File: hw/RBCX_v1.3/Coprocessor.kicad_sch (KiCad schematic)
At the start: 27 parts

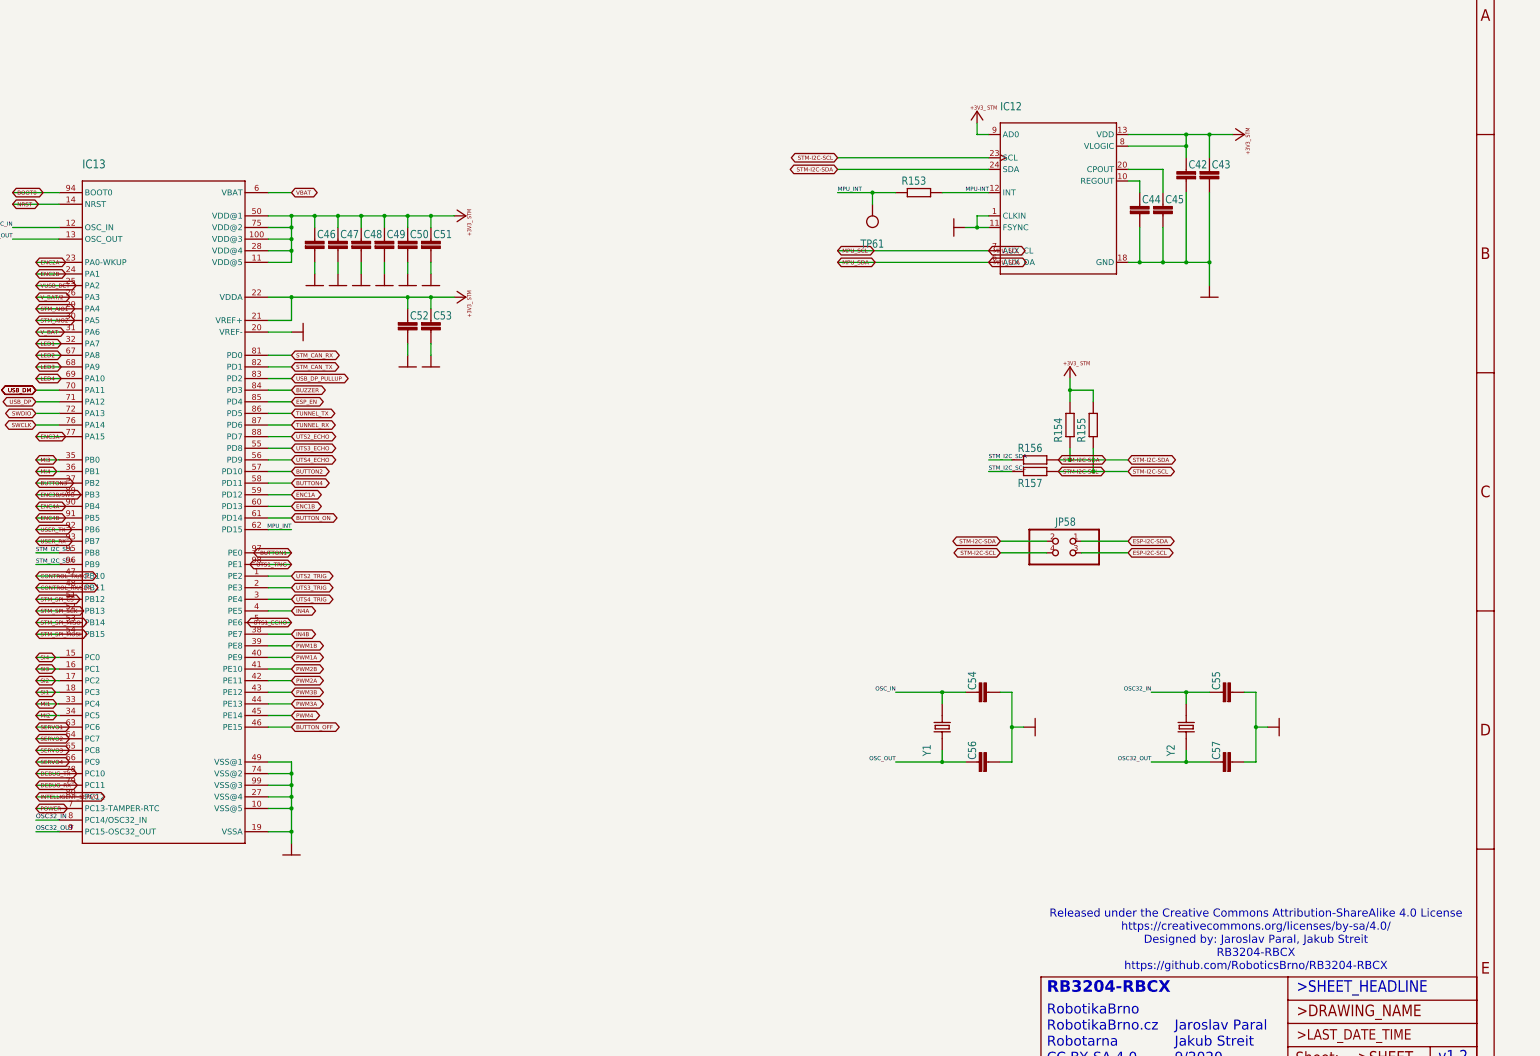
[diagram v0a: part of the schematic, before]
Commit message: Remove stepdowns, Micro-USB; fixup region names
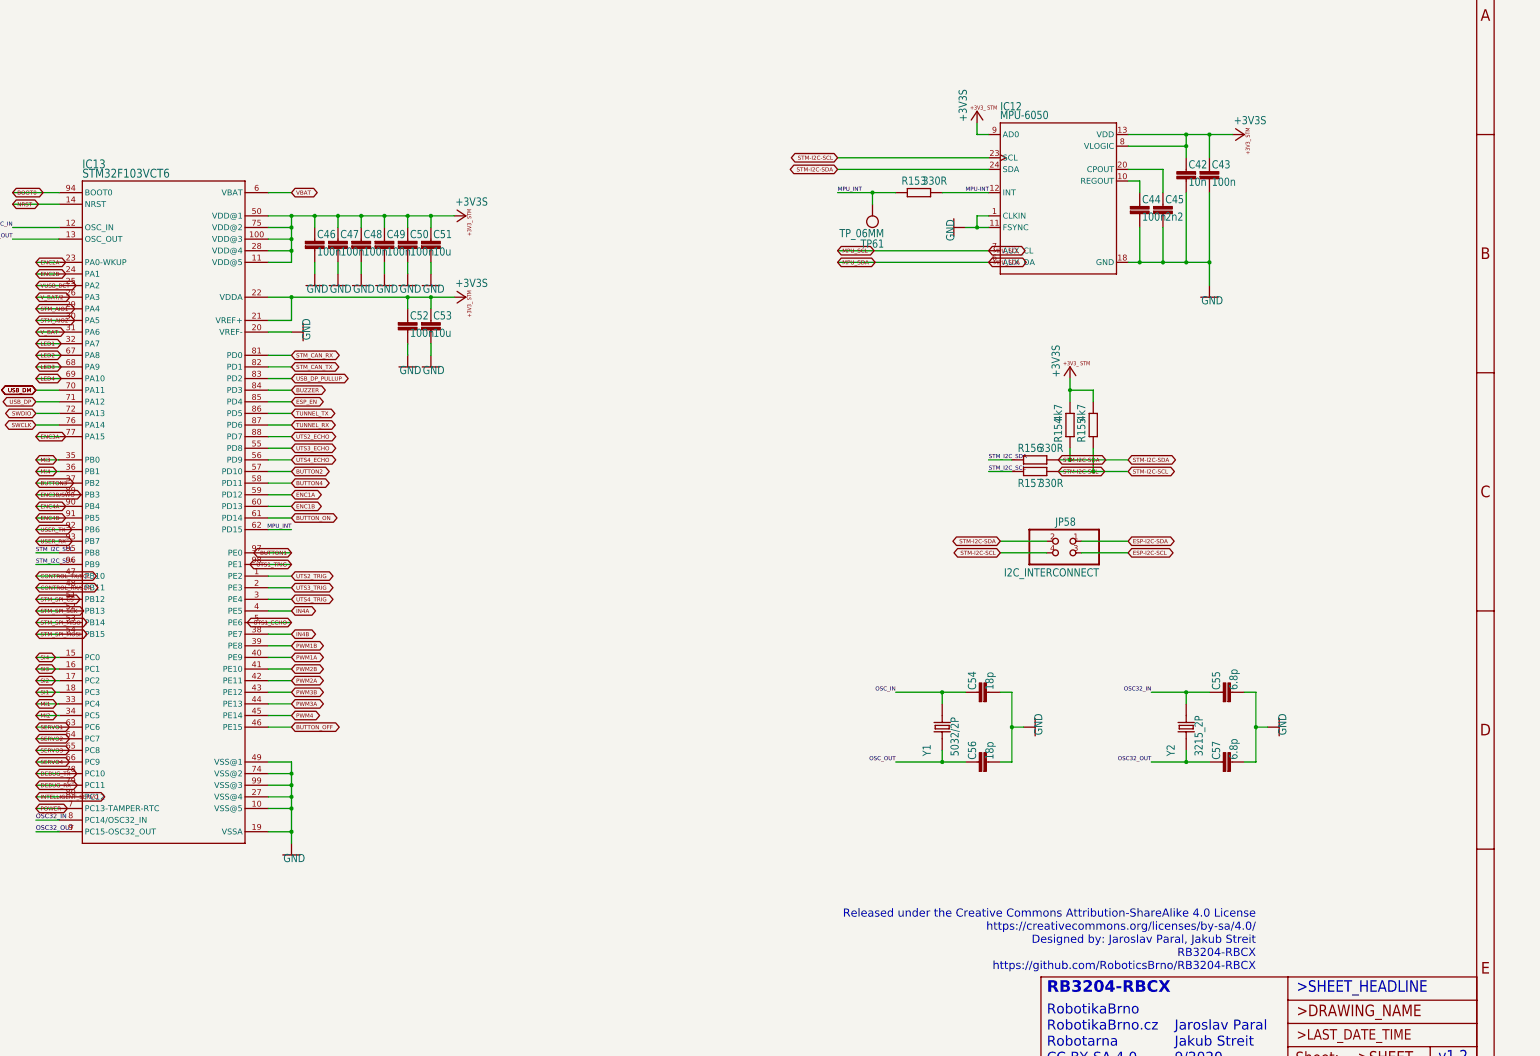
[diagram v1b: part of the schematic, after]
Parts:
- C42, C43, C44, C45, C46, C47, C48, C49, C50, C52, C54, C55, C56, C57: footprint (none) -> RBCX:C0402
- C51, C53: footprint (none) -> RBCX:C0805
- IC12: value (none) -> MPU-6050; footprint (none) -> RBCX:QFN50P400X400X95-24N
- IC13: value (none) -> STM32F103VCT6; footprint (none) -> RBCX:QFP50P1600X1600X160-100N_STM32F103VCT6
- JP58: value (none) -> I2C_INTERCONNECT; footprint (none) -> RBCX:2X02
- R153, R156, R157: value (none) -> 330R; footprint (none) -> RBCX:R0402
- R154, R155: value (none) -> 4k7; footprint (none) -> RBCX:R0402
- TP61: value (none) -> TP_06MM; footprint (none) -> RBCX:TP_06
- Y1: value (none) -> 5032/2P; footprint (none) -> RBCX:OSCCC500X320X135
- Y2: value (none) -> 3215_2P; footprint (none) -> RBCX:SMD-3215_2P
